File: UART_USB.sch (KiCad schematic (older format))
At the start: 6 parts, among them J4 USB_B_Mini, U19 CH330N, U20 LM1117-3.3

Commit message: reorganized schematic; added reverse polarity protection; start adding footprints
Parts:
- removed C16, C17, C18: C_Small, symbol Device:C_Small
- removed U19: CH330N, Package_SO:SOIC-8_3.9x4.9mm_P1.27mm, symbol Interface_USB:CH330N
- removed U20: LM1117-3.3, symbol Regulator_Linear:LM1117-3.3
- added C?: 4.7uF, symbol Device:C_Small
- added C? (x3): 100nF, symbol Device:C_Small
- added C?: 10nF, symbol Device:C_Small
- added D?: TXLED, symbol Device:LED
- added D?: RXLED, symbol Device:LED
- added L?: L, symbol Device:L
- added R? (x2): 10k, symbol Device:R
- added R?: 4k7, symbol Device:R
- added R? (x2): 1k, symbol Device:R
- added U?: FT232RL, Package_SO:SSOP-28_5.3x10.2mm_P0.65mm, symbol Interface_USB:FT232RL
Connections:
- net labels added: CTS, RTS, RXD, TXD
- net labels removed: UART_RX, UART_TX
- wire segments 22 -> 66
- no-connect marks 1 -> 7

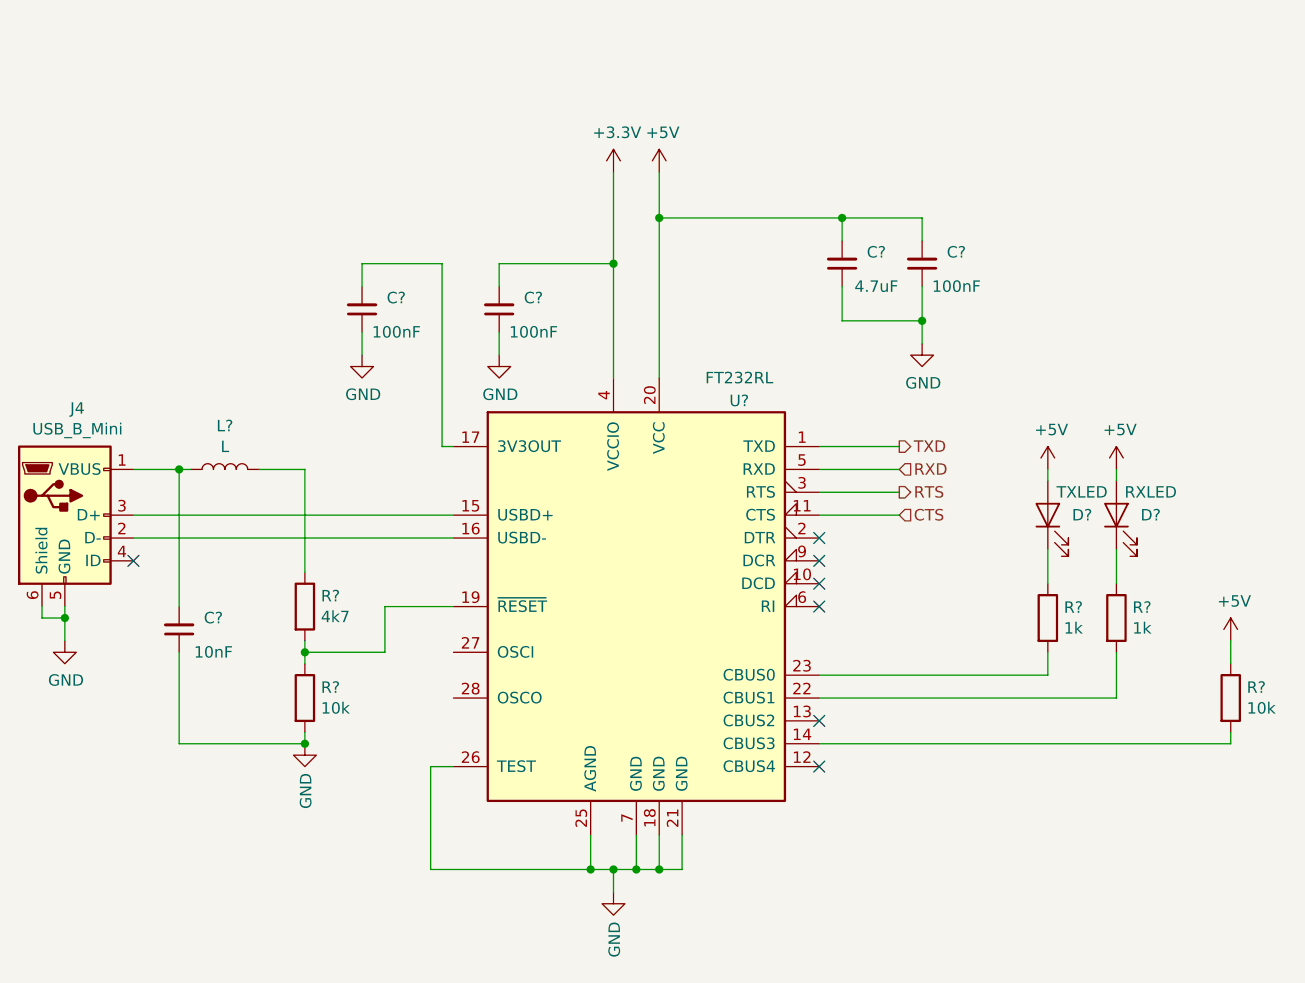
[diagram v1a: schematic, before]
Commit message: footprints; library for 7seg; start pcb layout
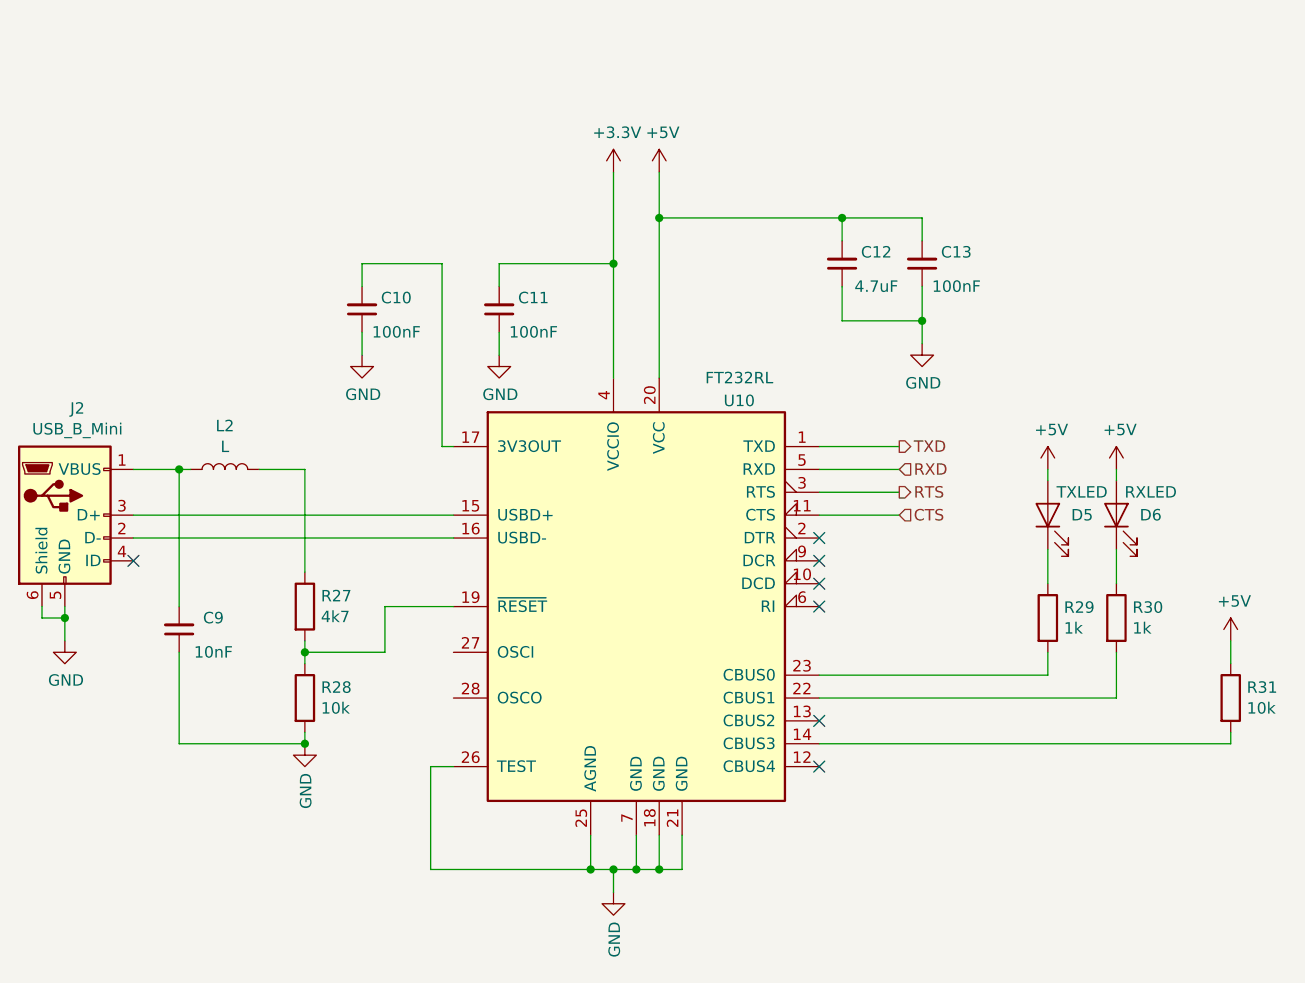
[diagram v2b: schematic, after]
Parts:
- C10, C11, C12, C13, C9: renamed from C?; footprint (none) -> Capacitor_SMD:C_0603_1608Metric
- D5, D6: renamed from D?; footprint (none) -> LED_SMD:LED_0603_1608Metric
- J2: renamed from J4; footprint (none) -> Connector_USB:USB_Mini-B_Lumberg_2486_01_Horizontal
- L2: renamed from L?; footprint (none) -> Inductor_SMD:L_0603_1608Metric
- R27, R28, R29, R30, R31: renamed from R?; footprint (none) -> Resistor_SMD:R_0603_1608Metric
- gave numbers to parts that had none: 1
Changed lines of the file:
@@
 $Descr A4 11693 8268
 encoding utf-8
-Sheet 6 9
+Sheet 4 9
 Title "PUTM_EV_Dashboard_2021"
 Date ""
@@
 $EndDescr
 $Comp
-L power:+5V #PWR0168
+L power:+5V #PWR031
 U 1 1 5FD44599
 P 6200 1400
-F 0 "#PWR0168" H 6200 1250 50  0001 C CNN
+F 0 "#PWR031" H 6200 1250 50  0001 C CNN
 F 1 "+5V" H 6215 1573 50  0000 C CNN
 F 2 "" H 6200 1400 50  0001 C CNN
@@
 $EndComp
 $Comp
-L dash_hw-rescue:USB_B_Mini-Connector J4
+L dash_hw-rescue:USB_B_Mini-Connector J?
 U 1 1 5FD44A28
 P 3600 2900
-AR Path="/5FD44A28" Ref="J4"  Part="1"
-AR Path="/5FD4381C/5FD44A28" Ref="J4"  Part="1"
-F 0 "J4" H 3655 3367 50  0000 C CNN
+AR Path="/5FD44A28" Ref="J?"  Part="1"
+AR Path="/5FD4381C/5FD44A28" Ref="J2"  Part="1"
+F 0 "J2" H 3655 3367 50  0000 C CNN
 F 1 "USB_B_Mini" H 3655 3276 50  0000 C CNN
-F 2 "" H 3750 2850 50  0001 C CNN
+F 2 "Connector_USB:USB_Mini-B_Lumberg_2486_01_Horizontal" H 3750 2850 50  0001 C CNN
 F 3 "~" H 3750 2850 50  0001 C CNN
 	1    3600 2900
@@
 $EndComp
 $Comp
-L power:GND #PWR0170
+L power:GND #PWR025
 U 1 1 5FD44A8C
 P 3600 3450
-F 0 "#PWR0170" H 3600 3200 50  0001 C CNN
+F 0 "#PWR025" H 3600 3200 50  0001 C CNN
 F 1 "GND" H 3605 3277 50  0000 C CNN
 F 2 "" H 3600 3450 50  0001 C CNN
@@
 	4150 2700 4100 2700
 $Comp
-L Interface_USB:FT232RL U?
+L Interface_USB:FT232RL U10
 U 1 1 5FD99CFA
 P 6100 3300
-F 0 "U?" H 6550 4200 50  0000 C CNN
+F 0 "U10" H 6550 4200 50  0000 C CNN
 F 1 "FT232RL" H 6550 4300 50  0000 C CNN
 F 2 "Package_SO:SSOP-28_5.3x10.2mm_P0.65mm" H 7200 2400 50  0001 C CNN
@@
 	3900 3000 5300 3000
 $Comp
-L Device:L L?
+L Device:L L2
 U 1 1 5FDA0F8F
 P 4300 2700
-F 0 "L?" V 4490 2700 50  0000 C CNN
+F 0 "L2" V 4490 2700 50  0000 C CNN
 F 1 "L" V 4399 2700 50  0000 C CNN
-F 2 "" H 4300 2700 50  0001 C CNN
+F 2 "Inductor_SMD:L_0603_1608Metric" H 4300 2700 50  0001 C CNN
 F 3 "~" H 4300 2700 50  0001 C CNN
 	1    4300 2700
@@
 $EndComp
 $Comp
-L Device:C_Small C?
+L Device:C_Small C12
 U 1 1 5FDA1B95
 P 7000 1800
-F 0 "C?" H 6850 1750 50  0000 C CNN
+F 0 "C12" H 6850 1750 50  0000 C CNN
 F 1 "4.7uF" H 6850 1900 50  0000 C CNN
-F 2 "" H 7000 1800 50  0001 C CNN
+F 2 "Capacitor_SMD:C_0603_1608Metric" H 7000 1800 50  0001 C CNN
 F 3 "~" H 7000 1800 50  0001 C CNN
 	1    7000 1800
@@
 $EndComp
 $Comp
-L Device:C_Small C?
+L Device:C_Small C13
 U 1 1 5FDA294E
 P 7350 1800
-F 0 "C?" H 7200 1750 50  0000 C CNN
+F 0 "C13" H 7200 1750 50  0000 C CNN
 F 1 "100nF" H 7200 1900 50  0000 C CNN
-F 2 "" H 7350 1800 50  0001 C CNN
+F 2 "Capacitor_SMD:C_0603_1608Metric" H 7350 1800 50  0001 C CNN
 F 3 "~" H 7350 1800 50  0001 C CNN
 	1    7350 1800
@@
 	7350 2050 7350 1900
 $Comp
-L power:GND #PWR?
+L power:GND #PWR032
 U 1 1 5FDA4EF3
 P 7350 2150
-F 0 "#PWR?" H 7350 1900 50  0001 C CNN
+F 0 "#PWR032" H 7350 1900 50  0001 C CNN
 F 1 "GND" H 7355 1977 50  0000 C CNN
 F 2 "" H 7350 2150 50  0001 C CNN
@@
 Connection ~ 6200 1600
 $Comp
-L Device:R R?
+L Device:R R28
 U 1 1 5FDA6A8A
 P 4650 3700
-F 0 "R?" H 4720 3746 50  0000 L CNN
+F 0 "R28" H 4720 3746 50  0000 L CNN
 F 1 "10k" H 4720 3655 50  0000 L CNN
-F 2 "" V 4580 3700 50  0001 C CNN
+F 2 "Resistor_SMD:R_0603_1608Metric" V 4580 3700 50  0001 C CNN
 F 3 "~" H 4650 3700 50  0001 C CNN
 	1    4650 3700
@@
 $EndComp
 $Comp
-L Device:R R?
+L Device:R R27
 U 1 1 5FDA7B86
 P 4650 3300
-F 0 "R?" H 4720 3346 50  0000 L CNN
+F 0 "R27" H 4720 3346 50  0000 L CNN
 F 1 "4k7" H 4720 3255 50  0000 L CNN
-F 2 "" V 4580 3300 50  0001 C CNN
+F 2 "Resistor_SMD:R_0603_1608Metric" V 4580 3300 50  0001 C CNN
 F 3 "~" H 4650 3300 50  0001 C CNN
 	1    4650 3300
@@
 	4650 3850 4650 3900
 $Comp
-L power:GND #PWR?
+L power:GND #PWR026
 U 1 1 5FDA9469
 P 4650 3900
-F 0 "#PWR?" H 4650 3650 50  0001 C CNN
+F 0 "#PWR026" H 4650 3650 50  0001 C CNN
 F 1 "GND" V 4655 3772 50  0000 R CNN
 F 2 "" H 4650 3900 50  0001 C CNN
@@
 $EndComp
 $Comp
-L Device:C_Small C?
+L Device:C_Small C10
 U 1 1 5FDAA5F5
 P 4900 2000
-F 0 "C?" H 4750 1950 50  0000 C CNN
+F 0 "C10" H 4750 1950 50  0000 C CNN
 F 1 "100nF" H 4750 2100 50  0000 C CNN
-F 2 "" H 4900 2000 50  0001 C CNN
+F 2 "Capacitor_SMD:C_0603_1608Metric" H 4900 2000 50  0001 C CNN
 F 3 "~" H 4900 2000 50  0001 C CNN
 	1    4900 2000
@@
 	4900 2100 4900 2200
 $Comp
-L power:GND #PWR?
+L power:GND #PWR027
 U 1 1 5FDAC004
 P 4900 2200
-F 0 "#PWR?" H 4900 1950 50  0001 C CNN
+F 0 "#PWR027" H 4900 1950 50  0001 C CNN
 F 1 "GND" H 4905 2027 50  0000 C CNN
 F 2 "" H 4900 2200 50  0001 C CNN
@@
 	6000 4450 6100 4450
 $Comp
-L power:GND #PWR?
+L power:GND #PWR030
 U 1 1 5FDAF1E2
 P 6000 4550
-F 0 "#PWR?" H 6000 4300 50  0001 C CNN
+F 0 "#PWR030" H 6000 4300 50  0001 C CNN
 F 1 "GND" V 6005 4422 50  0000 R CNN
 F 2 "" H 6000 4550 50  0001 C CNN
@@
 $EndComp
 $Comp
-L Device:C_Small C?
+L Device:C_Small C11
 U 1 1 5FDB28FC
 P 5500 2000
-F 0 "C?" H 5350 1950 50  0000 C CNN
+F 0 "C11" H 5350 1950 50  0000 C CNN
 F 1 "100nF" H 5350 2100 50  0000 C CNN
-F 2 "" H 5500 2000 50  0001 C CNN
+F 2 "Capacitor_SMD:C_0603_1608Metric" H 5500 2000 50  0001 C CNN
 F 3 "~" H 5500 2000 50  0001 C CNN
 	1    5500 2000
@@
 $EndComp
 $Comp
-L power:GND #PWR?
+L power:GND #PWR028
 U 1 1 5FDB2E56
 P 5500 2200
-F 0 "#PWR?" H 5500 1950 50  0001 C CNN
+F 0 "#PWR028" H 5500 1950 50  0001 C CNN
 F 1 "GND" H 5505 2027 50  0000 C CNN
 F 2 "" H 5500 2200 50  0001 C CNN
@@
 Connection ~ 6000 1800
 $Comp
-L power:+3.3V #PWR?
+L power:+3.3V #PWR029
 U 1 1 5FDB5730
 P 6000 1400
-F 0 "#PWR?" H 6000 1250 50  0001 C CNN
+F 0 "#PWR029" H 6000 1250 50  0001 C CNN
 F 1 "+3.3V" H 6015 1573 50  0000 C CNN
 F 2 "" H 6000 1400 50  0001 C CNN
@@
 $EndComp
 $Comp
-L Device:C_Small C?
+L Device:C_Small C9
 U 1 1 5FDB6776
 P 4100 3400
-F 0 "C?" H 3950 3350 50  0000 C CNN
+F 0 "C9" H 3950 3350 50  0000 C CNN
 F 1 "10nF" H 3950 3500 50  0000 C CNN
-F 2 "" H 4100 3400 50  0001 C CNN
+F 2 "Capacitor_SMD:C_0603_1608Metric" H 4100 3400 50  0001 C CNN
 F 3 "~" H 4100 3400 50  0001 C CNN
 	1    4100 3400
@@
 NoConn ~ 6900 3300
 $Comp
-L Device:R R?
+L Device:R R31
 U 1 1 5FDC3399
 P 8700 3700
-F 0 "R?" H 8770 3746 50  0000 L CNN
+F 0 "R31" H 8770 3746 50  0000 L CNN
 F 1 "10k" H 8770 3655 50  0000 L CNN
-F 2 "" V 8630 3700 50  0001 C CNN
+F 2 "Resistor_SMD:R_0603_1608Metric" V 8630 3700 50  0001 C CNN
 F 3 "~" H 8700 3700 50  0001 C CNN
 	1    8700 3700
@@
 	8700 3550 8700 3450
 $Comp
-L power:+5V #PWR?
+L power:+5V #PWR035
 U 1 1 5FDC673C
 P 8700 3450
-F 0 "#PWR?" H 8700 3300 50  0001 C CNN
+F 0 "#PWR035" H 8700 3300 50  0001 C CNN
 F 1 "+5V" H 8715 3623 50  0000 C CNN
 F 2 "" H 8700 3450 50  0001 C CNN
@@
 AR Path="/5FDCEDEB" Ref="D?"  Part="1"
 AR Path="/5FCC310D/5FDCEDEB" Ref="D?"  Part="1"
-AR Path="/5FD4381C/5FDCEDEB" Ref="D?"  Part="1"
-F 0 "D?" V 7900 2750 50  0000 C CNN
+AR Path="/5FD4381C/5FDCEDEB" Ref="D5"  Part="1"
+F 0 "D5" V 7900 2750 50  0000 C CNN
 F 1 "TXLED" V 8000 2750 50  0000 C CNN
-F 2 "" H 7900 2900 50  0001 C CNN
+F 2 "LED_SMD:LED_0603_1608Metric" H 7900 2900 50  0001 C CNN
 F 3 "~" H 7900 2900 50  0001 C CNN
 	1    7900 2900
@@
 AR Path="/5FDCFC14" Ref="D?"  Part="1"
 AR Path="/5FCC310D/5FDCFC14" Ref="D?"  Part="1"
-AR Path="/5FD4381C/5FDCFC14" Ref="D?"  Part="1"
-F 0 "D?" V 8200 2750 50  0000 C CNN
+AR Path="/5FD4381C/5FDCFC14" Ref="D6"  Part="1"
+F 0 "D6" V 8200 2750 50  0000 C CNN
 F 1 "RXLED" V 8300 2750 50  0000 C CNN
-F 2 "" H 8200 2900 50  0001 C CNN
+F 2 "LED_SMD:LED_0603_1608Metric" H 8200 2900 50  0001 C CNN
 F 3 "~" H 8200 2900 50  0001 C CNN
 	1    8200 2900
@@
 $EndComp
 $Comp
-L Device:R R?
+L Device:R R29
 U 1 1 5FDD4052
 P 7900 3350
-F 0 "R?" H 7970 3396 50  0000 L CNN
+F 0 "R29" H 7970 3396 50  0000 L CNN
 F 1 "1k" H 7970 3305 50  0000 L CNN
-F 2 "" V 7830 3350 50  0001 C CNN
+F 2 "Resistor_SMD:R_0603_1608Metric" V 7830 3350 50  0001 C CNN
 F 3 "~" H 7900 3350 50  0001 C CNN
 	1    7900 3350
@@
 $EndComp
 $Comp
-L Device:R R?
+L Device:R R30
 U 1 1 5FDD4CED
 P 8200 3350
-F 0 "R?" H 8270 3396 50  0000 L CNN
+F 0 "R30" H 8270 3396 50  0000 L CNN
 F 1 "1k" H 8270 3305 50  0000 L CNN
-F 2 "" V 8130 3350 50  0001 C CNN
+F 2 "Resistor_SMD:R_0603_1608Metric" V 8130 3350 50  0001 C CNN
 F 3 "~" H 8200 3350 50  0001 C CNN
 	1    8200 3350
@@
 	8200 2750 8200 2700
 $Comp
-L power:+5V #PWR?
+L power:+5V #PWR033
 U 1 1 5FDDBF60
 P 7900 2700
-F 0 "#PWR?" H 7900 2550 50  0001 C CNN
+F 0 "#PWR033" H 7900 2550 50  0001 C CNN
 F 1 "+5V" H 7915 2873 50  0000 C CNN
 F 2 "" H 7900 2700 50  0001 C CNN
@@
 $EndComp
 $Comp
-L power:+5V #PWR?
+L power:+5V #PWR034
 U 1 1 5FDDC9E8
 P 8200 2700
-F 0 "#PWR?" H 8200 2550 50  0001 C CNN
+F 0 "#PWR034" H 8200 2550 50  0001 C CNN
 F 1 "+5V" H 8215 2873 50  0000 C CNN
 F 2 "" H 8200 2700 50  0001 C CNN

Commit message: Hardware update Approved
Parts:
- L2: value L -> KoralikFerrytowy
- R29, R30: value 1k -> 560R
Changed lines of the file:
@@
 EESchema Schematic File Version 4
+LIBS:dash_hw-cache
 EELAYER 30 0
 EELAYER END
@@
 P 4300 2700
 F 0 "L2" V 4490 2700 50  0000 C CNN
-F 1 "L" V 4399 2700 50  0000 C CNN
+F 1 "KoralikFerrytowy" V 4399 2700 50  0000 C CNN
 F 2 "Inductor_SMD:L_0603_1608Metric" H 4300 2700 50  0001 C CNN
 F 3 "~" H 4300 2700 50  0001 C CNN
@@
 P 7900 3350
 F 0 "R29" H 7970 3396 50  0000 L CNN
-F 1 "1k" H 7970 3305 50  0000 L CNN
+F 1 "560R" H 7970 3305 50  0000 L CNN
 F 2 "Resistor_SMD:R_0603_1608Metric" V 7830 3350 50  0001 C CNN
 F 3 "~" H 7900 3350 50  0001 C CNN
@@
 P 8200 3350
 F 0 "R30" H 8270 3396 50  0000 L CNN
-F 1 "1k" H 8270 3305 50  0000 L CNN
+F 1 "560R" H 8270 3305 50  0000 L CNN
 F 2 "Resistor_SMD:R_0603_1608Metric" V 8130 3350 50  0001 C CNN
 F 3 "~" H 8200 3350 50  0001 C CNN
